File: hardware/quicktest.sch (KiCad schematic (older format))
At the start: 48 parts, among them J1 USB_OTG, J2 Vibration Motor, J3 CONN_02X03, Q1 PMOS_2.5A/30V, Q2 2N2222, SW1 SW_Push, SW2 SW_Push, SW3 SW_Push, U1 DS3231MZ, U2 ATMEGA328P-AU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

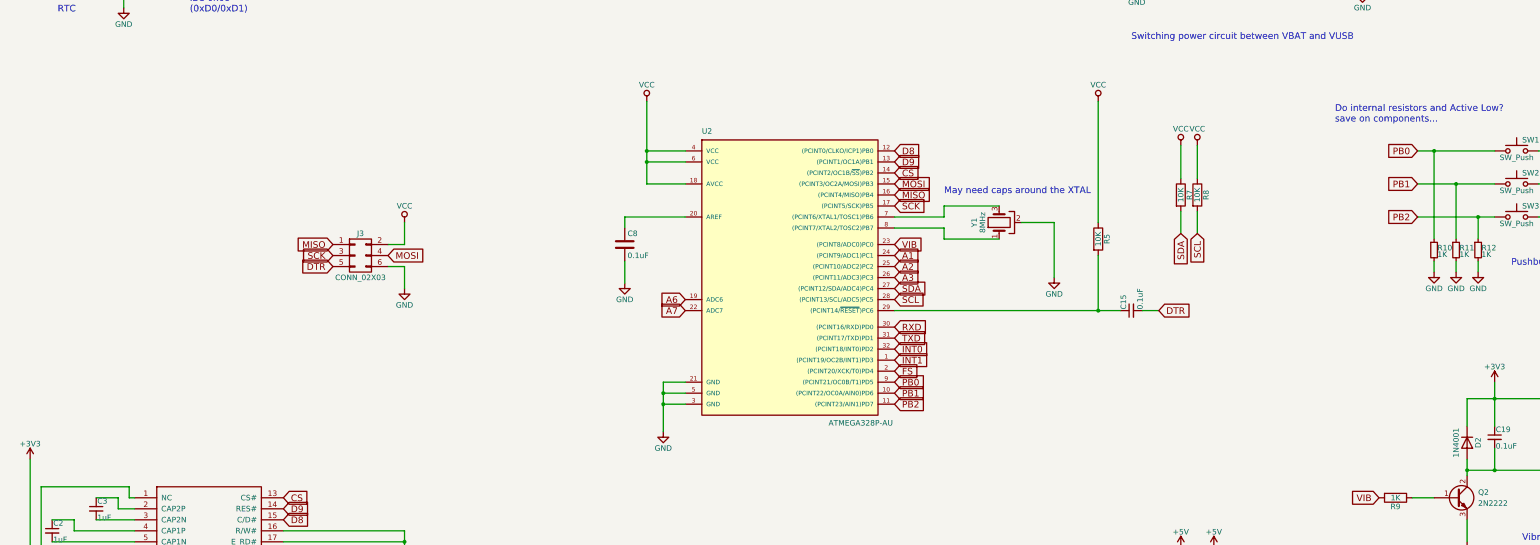
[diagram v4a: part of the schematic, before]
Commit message: decided to start with a light version of the watch, have been working on that schematic and pcb
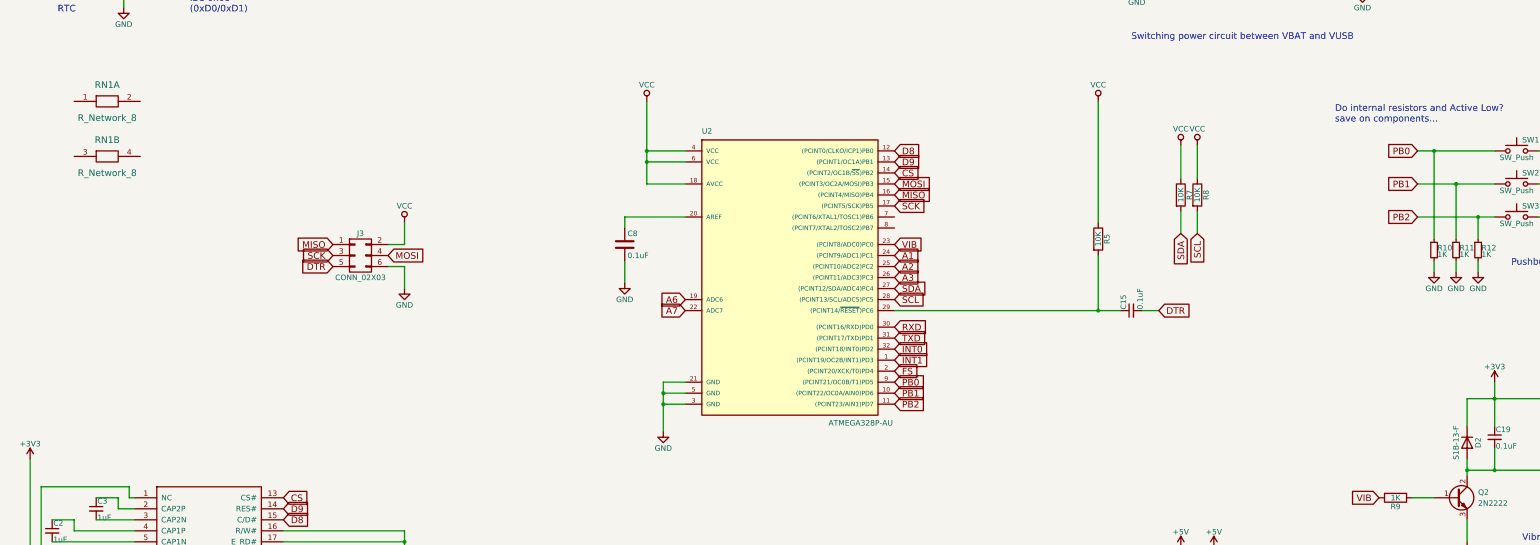
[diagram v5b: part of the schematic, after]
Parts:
- removed Y1: 8MHz, Crystals:Crystal_SMD_SeikoEpson_MA506-4pin_12.7x5.1mm, symbol Crystal_GND2
- added RN1: R_Network_8, Housings_SSOP:SSOP-16_3.9x4.9mm_Pitch0.635mm, symbol R_Network_8
- D2: value 1N4001 -> S1B-13-F; footprint Diodes_THT:D_DO-41_SOD81_P10.16mm_Horizontal -> Diodes_SMD:D_SMA
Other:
- note removed: "May need caps around the XTAL"
